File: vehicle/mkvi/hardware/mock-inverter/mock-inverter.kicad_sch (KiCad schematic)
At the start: 64 parts, among them J1 MicroFit_RA_4, J2 TagConnect_6, J3 MicroFit_RA_3, K1 3350-4275, U1 MAX7221CWG_1, U2 ATMEGA16M1, U3 TLV76780DBVR, U4 MCP2561-E_SN, U5 ADUM4150ARIZ-RL, U6 ADS7816U, Y1 Crystal_SMD

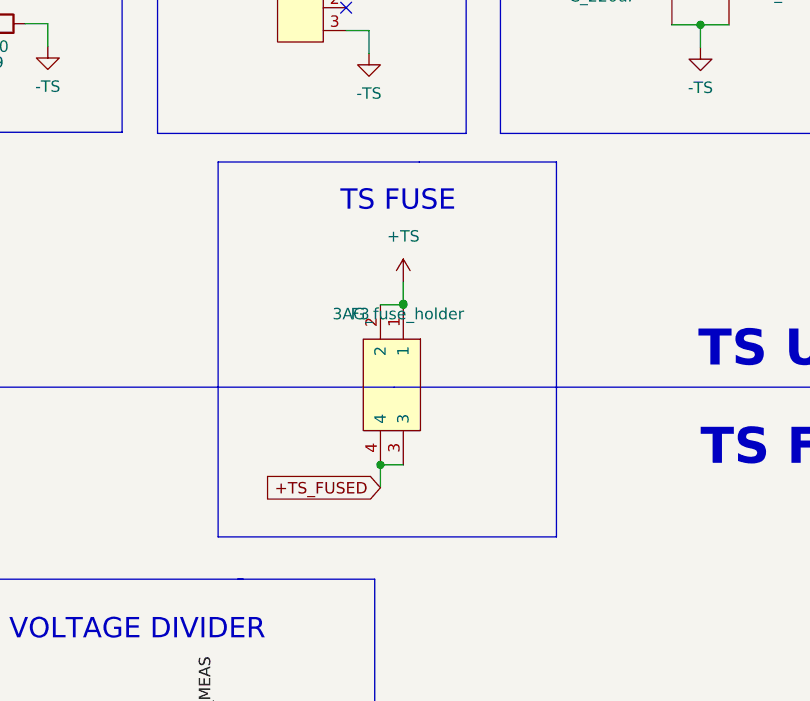
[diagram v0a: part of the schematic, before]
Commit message: Fix additional symbols in symbol library
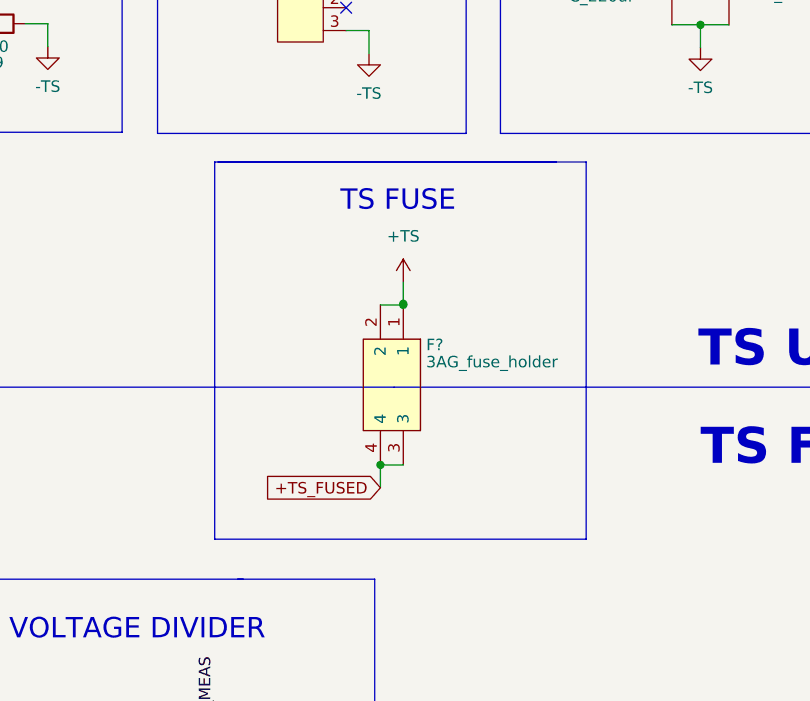
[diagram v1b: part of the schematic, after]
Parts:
- removed F3: 3AG_fuse_holder, footprints:4245, symbol formula:3AG_fuse_holder
- added F?: 3AG_fuse_holder, footprints:4245, symbol formula:3AG_fuse_holder_1
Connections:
- net +5V: now also F?.1, F?.2
- net +TS_FUSED: now also F?.3, F?.4
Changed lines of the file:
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@@
   (junction (at 50.8 169.545) (diameter 0) (color 0 0 0 0)
   )
-  (junction (at 182.88 40.64) (diameter 0) (color 0 0 0 0)
-  )
   (junction (at 335.28 87.63) (diameter 0) (color 0 0 0 0)
   )
+  (junction (at 182.88 40.64) (diameter 0) (color 0 0 0 0)
+  )
   (junction (at 36.195 159.385) (diameter 0) (color 0 0 0 0)
   )
@@
   (junction (at 220.345 180.34) (diameter 0) (color 0 0 0 0)
   )
+  (junction (at 332.74 105.41) (diameter 0) (color 0 0 0 0)
+  )
   (junction (at 106.68 110.49) (diameter 0) (color 0 0 0 0)
   )
@@
   (junction (at 250.19 180.34) (diameter 0) (color 0 0 0 0)
   )
-  (junction (at 332.74 105.41) (diameter 0) (color 0 0 0 0)
-  )
   (junction (at 302.514 175.387) (diameter 0) (color 0 0 0 0)
   )
@@
     (stroke (width 0) (type default) (color 0 0 0 0))
   )
-  (polyline (pts (xy 352.298 113.411) (xy 314.706 113.411))
-    (stroke (width 0) (type default) (color 0 0 0 0))
-  )
   (polyline (pts (xy 85.725 234.95) (xy 16.51 234.95))
     (stroke (width 0) (type default) (color 0 0 0 0))
@@
     (stroke (width 0) (type default) (color 0 0 0 0))
   )
+  (polyline (pts (xy 314.325 71.755) (xy 351.155 71.755))
+    (stroke (width 0) (type default) (color 0 0 0 0))
+  )
   (polyline (pts (xy 324.739 158.242) (xy 353.949 158.242))
     (stroke (width 0) (type default) (color 0 0 0 0))
@@
     (stroke (width 0) (type default) (color 0 0 0 0))
   )
+  (polyline (pts (xy 355.6 113.665) (xy 314.325 113.665))
+    (stroke (width 0) (type default) (color 0 0 0 0))
+  )
   (polyline (pts (xy 275.971 227.076) (xy 275.971 204.851))
     (stroke (width 0) (type default) (color 0 0 0 0))
@@
     (stroke (width 0) (type default) (color 0 0 0 0))
   )
-  (polyline (pts (xy 352.298 71.755) (xy 352.298 113.411))
-    (stroke (width 0) (type default) (color 0 0 0 0))
-  )
   (polyline (pts (xy 164.211 145.542) (xy 185.166 145.542))
     (stroke (width 0) (type default) (color 0 0 0 0))
@@
     (stroke (width 0) (type default) (color 0 0 0 0))
   )
+  (polyline (pts (xy 355.6 71.755) (xy 355.6 113.665))
+    (stroke (width 0) (type default) (color 0 0 0 0))
+  )
   (polyline (pts (xy 148.59 254.635) (xy 148.59 220.345))
     (stroke (width 0) (type default) (color 0 0 0 0))
@@
     (stroke (width 0) (type default) (color 0 0 0 0))
   )
-  (polyline (pts (xy 314.706 113.411) (xy 314.706 71.755))
-    (stroke (width 0) (type default) (color 0 0 0 0))
-  )
   (polyline (pts (xy 133.35 16.51) (xy 133.35 24.13))
     (stroke (width 0) (type default) (color 0 0 0 0))
@@
     (stroke (width 0) (type default) (color 0 0 0 0))
   )
+  (polyline (pts (xy 314.325 113.665) (xy 314.325 71.755))
+    (stroke (width 0) (type default) (color 0 0 0 0))
+  )
   (polyline (pts (xy 158.115 73.025) (xy 180.34 73.025))
     (stroke (width 0) (type default) (color 0 0 0 0))
@@
     (stroke (width 0) (type default) (color 0 0 0 0))
   )
+  (polyline (pts (xy 351.155 71.755) (xy 355.6 71.755))
+    (stroke (width 0) (type default) (color 0 0 0 0))
+  )
   (wire (pts (xy 246.38 126.365) (xy 250.19 126.365))
     (stroke (width 0) (type default) (color 0 0 0 0))
@@
     (pin "1")
   )
-  (symbol (lib_name "3AG_fuse_holder_1") (lib_id "formula:3AG_fuse_holder") (at 335.28 86.36 270) (unit 1)
-    (in_bom yes) (on_board yes)
-    (property "Reference" "F3" (id 0) (at 329.438 88.646 90)
-      (effects (font (size 1.27 1.27)) (justify left))
-    )
-    (property "Value" "3AG_fuse_holder" (id 1) (at 327.406 88.646 90)
-      (effects (font (size 1.27 1.27)) (justify left))
-    )
-    (property "Footprint" "footprints:4245" (id 2) (at 309.88 63.5 0)
-      (effects (font (size 1.27 1.27)) (justify left) hide)
-    )
-    (property "Datasheet" "https://www.keyelco.com/product-pdf.cfm?p=322" (id 3) (at 312.42 63.5 0)
-      (effects (font (size 1.27 1.27)) (justify left) hide)
-    )
-    (property "Description" "Hldr, Fuse; Brass; PCB Mount; 1347 in. L x 0.285 in. W; Clips; UL Listed" (id 4) (at 314.96 63.5 0)
-      (effects (font (size 1.27 1.27)) (justify left) hide)
-    )
-    (property "Height" "13" (id 5) (at 317.5 63.5 0)
-      (effects (font (size 1.27 1.27)) (justify left) hide)
-    )
-    (property "Manufacturer_Part_Number" "4245" (id 6) (at 322.58 63.5 0)
-      (effects (font (size 1.27 1.27)) (justify left) hide)
-    )
-    (property "Digikey Part Number" "36-4245-ND" (id 7) (at 325.12 63.5 0)
-      (effects (font (size 1.27 1.27)) (justify left) hide)
-    )
-    (property "PurchasingLink" "https://www.digikey.com/en/products/detail/keystone-electronics/4245/316165" (id 8) (at 328.295 23.495 0)
-      (effects (font (size 1.27 1.27)) hide)
-    )
-    (property "FuseMPN" "https://www.digikey.com/en/products/detail/bel-fuse-inc/0ADBC0200-BE/8028431" (id 9) (at 335.28 86.36 0)
-      (effects (font (size 1.27 1.27)) hide)
-    )
-    (property "FusePurchasingLink" "https://www.digikey.com/en/products/detail/bel-fuse-inc/0ADBC0200-BE/8028431" (id 10) (at 335.28 86.36 0)
-      (effects (font (size 1.27 1.27)) hide)
-    )
-    (pin "1")
-    (pin "2")
-    (pin "3")
-    (pin "4")
-  )
   (symbol (lib_id "Device:R") (at 308.61 143.51 270) (unit 1)
     (in_bom yes) (on_board yes)
@@
     (pin "2")
   )
+  (symbol (lib_id "formula:3AG_fuse_holder_1") (at 335.28 86.36 270) (unit 1)
+    (in_bom yes) (on_board yes)
+    (property "Reference" "F?" (id 0) (at 337.82 92.075 90)
+      (effects (font (size 1.27 1.27)) (justify left))
+    )
+    (property "Value" "3AG_fuse_holder" (id 1) (at 337.82 93.98 90)
+      (effects (font (size 1.27 1.27)) (justify left))
+    )
+    (property "Footprint" "footprints:4245" (id 2) (at 309.88 63.5 0)
+      (effects (font (size 1.27 1.27)) (justify left) hide)
+    )
+    (property "Datasheet" "https://www.keyelco.com/product-pdf.cfm?p=322" (id 3) (at 312.42 63.5 0)
+      (effects (font (size 1.27 1.27)) (justify left) hide)
+    )
+    (property "Description" "Hldr, Fuse; Brass; PCB Mount; 1347 in. L x 0.285 in. W; Clips; UL Listed" (id 4) (at 314.96 63.5 0)
+      (effects (font (size 1.27 1.27)) (justify left) hide)
+    )
+    (property "Height" "13" (id 5) (at 317.5 63.5 0)
+      (effects (font (size 1.27 1.27)) (justify left) hide)
+    )
+    (property "Manufacturer_Part_Number" "4245" (id 6) (at 322.58 63.5 0)
+      (effects (font (size 1.27 1.27)) (justify left) hide)
+    )
+    (property "Digikey Part Number" "36-4245-ND" (id 7) (at 325.12 63.5 0)
+      (effects (font (size 1.27 1.27)) (justify left) hide)
+    )
+    (property "PurchasingLink" "https://www.digikey.com/en/products/detail/keystone-electronics/4245/316165" (id 8) (at 328.295 23.495 0)
+      (effects (font (size 1.27 1.27)) hide)
+    )
+    (property "FuseMPN" "https://www.digikey.com/en/products/detail/bel-fuse-inc/0ADBC0200-BE/8028431" (id 9) (at 335.28 86.36 0)
+      (effects (font (size 1.27 1.27)) hide)
+    )
+    (property "FusePurchasingLink" "https://www.digikey.com/en/products/detail/bel-fuse-inc/0ADBC0200-BE/8028431" (id 10) (at 335.28 86.36 0)
+      (effects (font (size 1.27 1.27)) hide)
+    )
+    (pin "1")
+    (pin "2")
+    (pin "3")
+    (pin "4")
+  )
   (symbol (lib_name "TLV76780DBVR_1") (lib_id "formula:TLV76780DBVR") (at 50.8 160.02 0) (unit 1)
     (in_bom yes) (on_board yes) (fields_autoplaced)
@@
       (reference "F2") (unit 1) (value "F_2A_16V") (footprint "footprints:Fuse_1812_4532Metric")
     )
-    (path "/6746478a-5db0-4370-a700-675894982fe7"
-      (reference "F3") (unit 1) (value "3AG_fuse_holder") (footprint "footprints:4245")
+    (path "/8fe491a3-0f0f-4aaf-acc8-6292887f8cc5"
+      (reference "F?") (unit 1) (value "3AG_fuse_holder") (footprint "footprints:4245")
     )
     (path "/cc76d178-27f2-4db1-9851-5d5d347a01cd"
